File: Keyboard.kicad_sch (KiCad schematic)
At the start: 16 parts, among them J1 USB_mini_micro_B, SW1 SW_PUSH, U1 ATMEGA32U4, X1 XTAL_GND

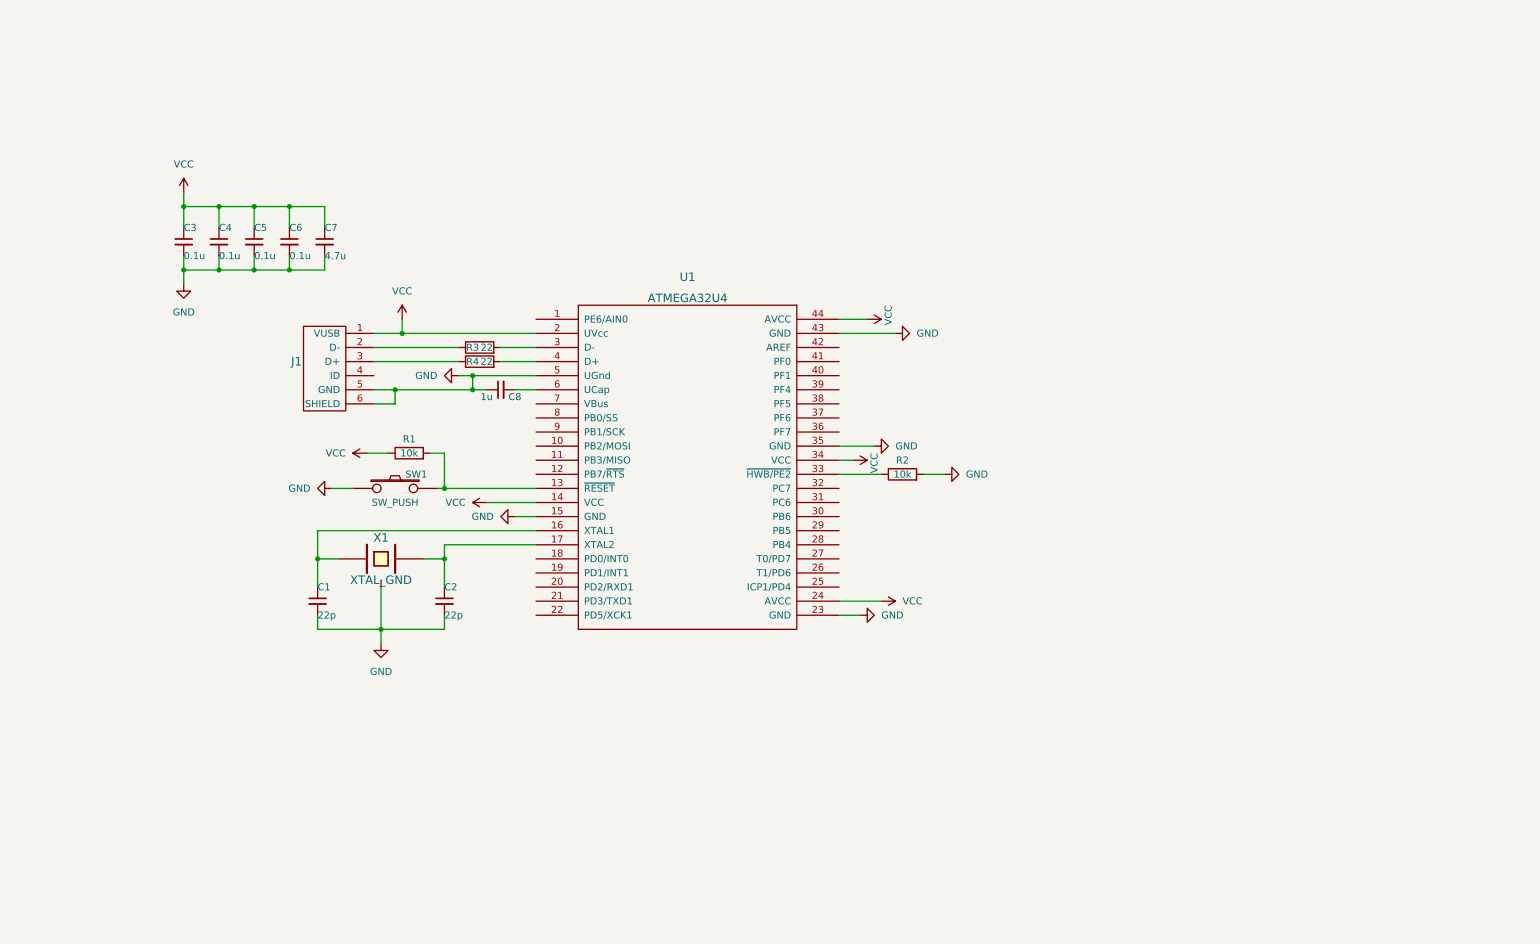
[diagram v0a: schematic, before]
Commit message: Added a TQFP pakcage version
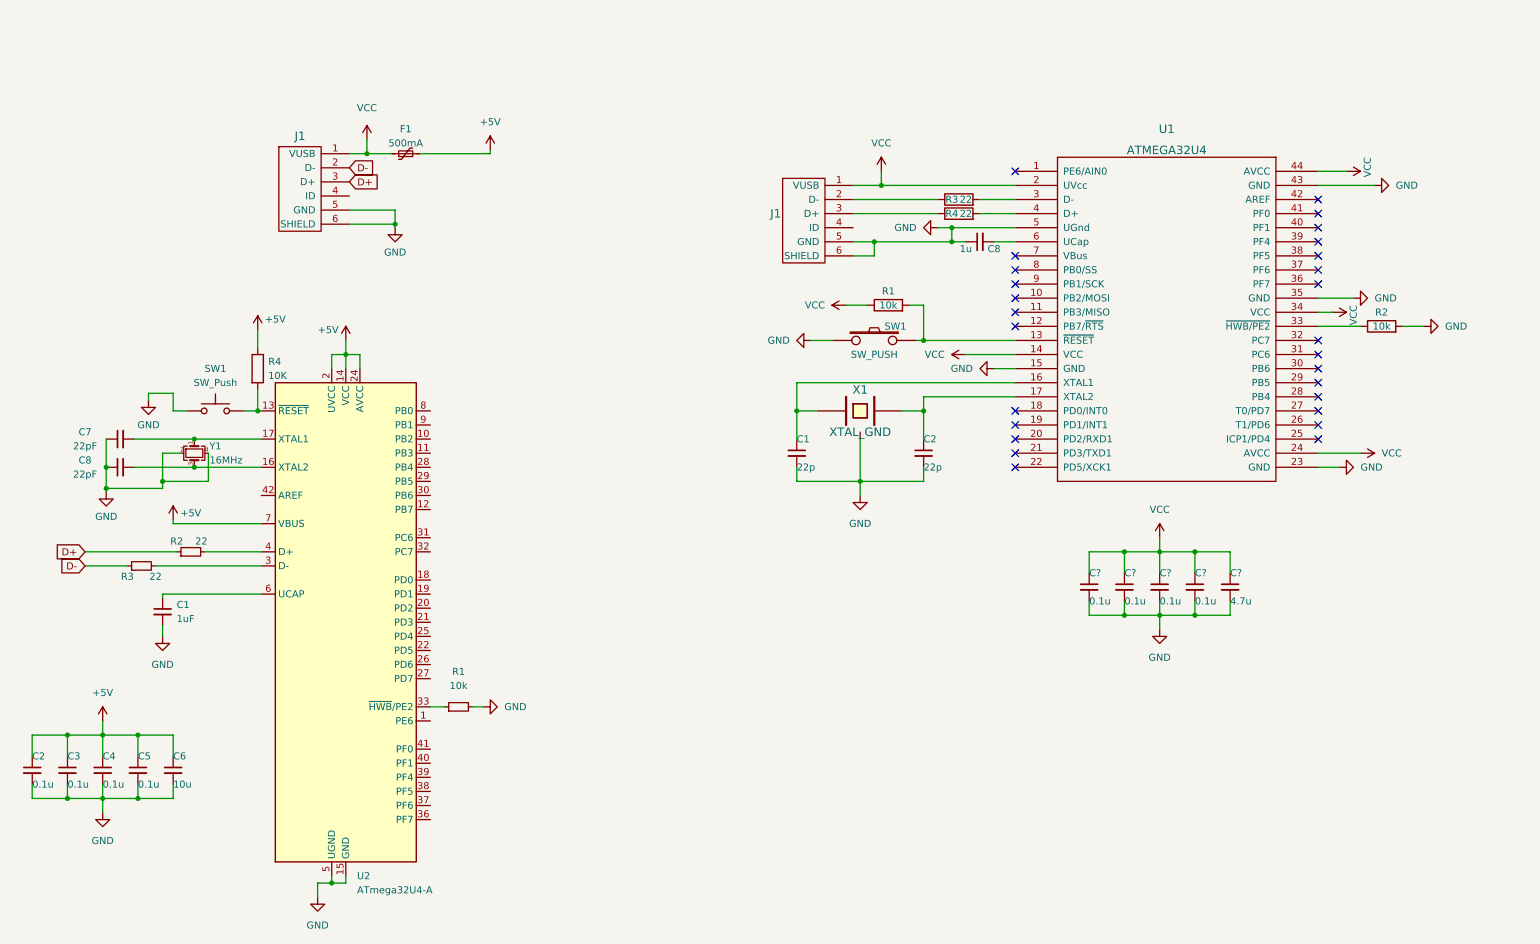
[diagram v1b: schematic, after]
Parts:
- added C1: 1uF, symbol Device:C_Small
- added C7, C8: 22pF, symbol Device:C_Small
- added C? (x4): 0.1u, symbol Device:C_Small
- added C?: 4.7u, symbol Device:C_Small
- added F1: 500mA, symbol Device:Polyfuse_Small
- added J1: USB_mini_micro_B, symbol keyboard_parts:USB_mini_micro_B
- added R1: 10k, symbol Device:R_Small
- added R2, R3: 22, symbol Device:R_Small
- added R4: 10K, symbol Device:R
- added SW1: SW_Push, symbol Switch:SW_Push
- added U2: ATmega32U4-A, Package_QFP:TQFP-44_10x10mm_P0.8mm, symbol MCU_Microchip_ATmega:ATmega32U4-A
- added Y1: 16MHz, symbol Device:Crystal_GND24_Small
- C6: renamed from C7; value 4.7u -> 10u
- renumbered C3 to C2, C4 to C3, C5 to C4, C6 to C5
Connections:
- net GND: now also C1.2, C7.1, C8.1, C?.2, C?.2, C?.2, C?.2, C?.2, J1.5 (GND), J1.6 (SHIELD), R1.2, SW1.1, U2.15 (GND), U2.23 (GND), U2.35 (GND), U2.43 (GND), U2.5 (UGND), Y1.2, Y1.4
- net VCC: now also C?.1, C?.1, C?.1, C?.1, C?.1, F1.1, J1.1 (VUSB); no longer C2.1, C3.1, C4.1, C5.1, C6.1
- new net: C7.2, U2.17 (XTAL1), Y1.1
- new net: R1.1, U2.33 (~{HWB}/PE2)
- new net: C8.2, U2.16 (XTAL2), Y1.3
- new net: R3.2, U2.3 (D-)
- new net: R2.2, U2.4 (D+)
- new net: R4.2, SW1.2, U2.13 (~{RESET})
- new net: C1.1, U2.6 (UCAP)
- new net +5V: C2.1, C3.1, C4.1, C5.1, C6.1, F1.2, R4.1, U2.14 (VCC), U2.2 (UVCC), U2.24 (AVCC), U2.34 (VCC), U2.44 (AVCC), U2.7 (VBUS)
- new net D+: J1.3 (D+), R2.1
- new net D-: J1.2 (D-), R3.1
- no-connect marks 0 -> 27
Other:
- moved on the sheet: C1, C2, C3, C4, C5, C6, C8, J1, R1, R2, R3, R4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

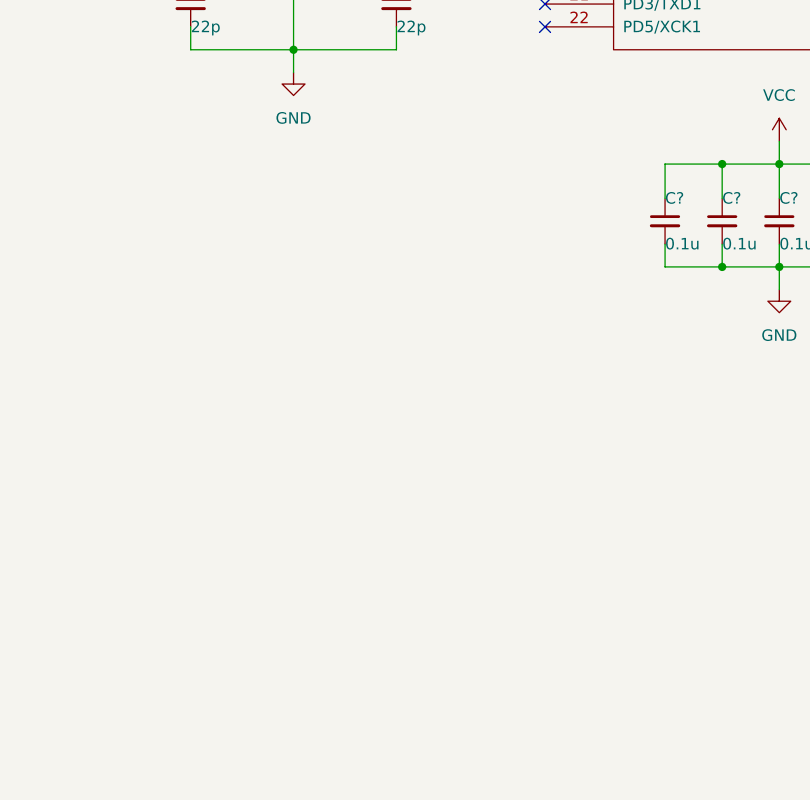
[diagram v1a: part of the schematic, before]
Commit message: Created Matrix file and added row and column wires
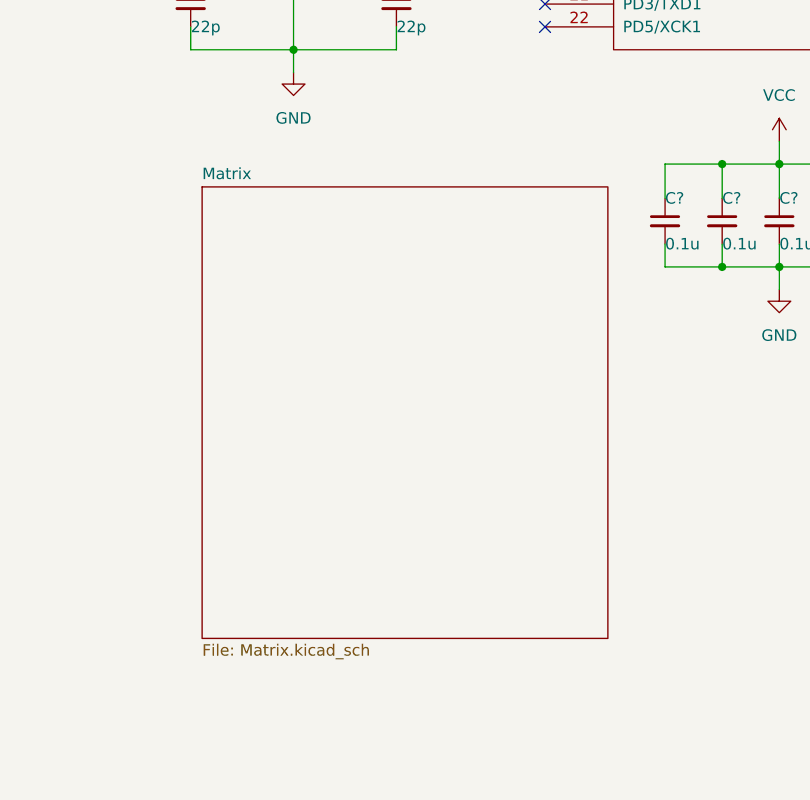
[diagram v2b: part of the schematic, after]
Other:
- added sheet Matrix (Matrix.kicad_sch)
- title: (none) -> main
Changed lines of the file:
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@@
 (kicad_sch (version 20211123) (generator eeschema)
   (paper "A4")
+  (title_block
+    (title "main")
+    (date "2022-08-09")
+    (rev "0")
+  )
   (junction (at 184.15 55.88) (diameter 0) (color 0 0 0 0)
   )
@@
     (pin "1")
   )
+  (sheet (at 157.48 114.3) (size 45.085 50.165) (fields_autoplaced)
+    (stroke (width 0.1524) (type solid) (color 0 0 0 0))
+    (fill (color 0 0 0 0.0000))
+    (property "Sheet name" "Matrix" (id 0) (at 157.48 113.5884 0)
+      (effects (font (size 1.27 1.27)) (justify left bottom))
+    )
+    (property "Sheet file" "Matrix.kicad_sch" (id 1) (at 157.48 165.0496 0)
+      (effects (font (size 1.27 1.27)) (justify left top))
+    )
+  )
   (sheet_instances
     (path "/" (page "1"))
+    (path "/c5d81d57-8916-4e7f-9cc3-b319fec74392" (page "2"))
   )
   (symbol_instances
@@
       (reference "C?") (unit 1) (value "0.1u") (footprint "")
     )
+    (path "/c5d81d57-8916-4e7f-9cc3-b319fec74392/6d39889c-9e2f-442a-a8e6-b65863b08f69"
+      (reference "D01") (unit 1) (value "1N4148") (footprint "")
+    )
     (path "/8545084e-b220-45d1-80e6-3744a0b67635"
       (reference "F1") (unit 1) (value "500mA") (footprint "")
@@
       (reference "R4") (unit 1) (value "10K") (footprint "")
     )
+    (path "/c5d81d57-8916-4e7f-9cc3-b319fec74392/0bbc6e45-febf-45ff-a858-5bf31f0a0486"
+      (reference "S01") (unit 1) (value "MX1A") (footprint "")
+    )
     (path "/6a7d6a80-4460-4050-abc5-328a82645129"

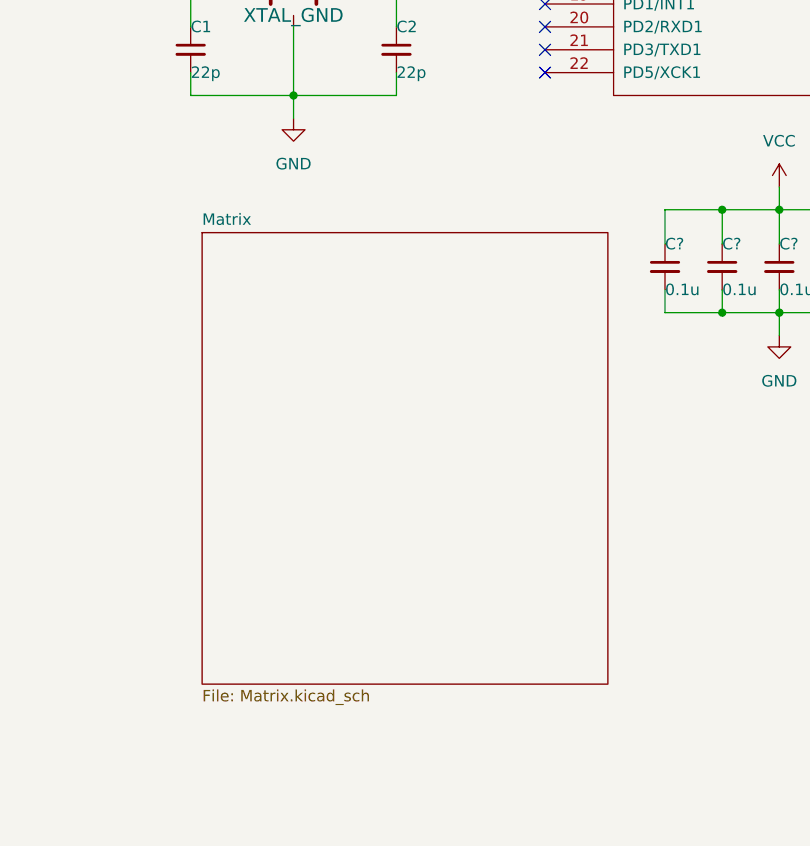
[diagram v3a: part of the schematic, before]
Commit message: Added key labels signifiying where each key will go to the matrix
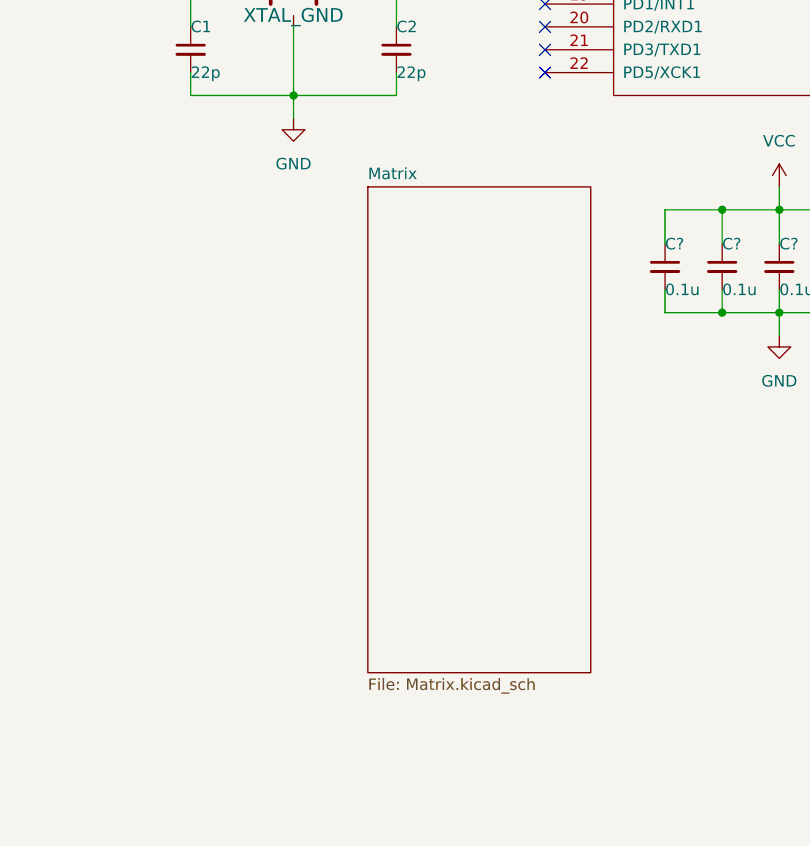
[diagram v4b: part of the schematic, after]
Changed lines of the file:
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@@
     (pin "1")
   )
-  (sheet (at 157.48 114.3) (size 45.085 50.165) (fields_autoplaced)
+  (sheet (at 175.895 109.22) (size 24.765 53.975) (fields_autoplaced)
     (stroke (width 0.1524) (type solid) (color 0 0 0 0))
     (fill (color 0 0 0 0.0000))
-    (property "Sheet name" "Matrix" (id 0) (at 157.48 113.5884 0)
+    (property "Sheet name" "Matrix" (id 0) (at 175.895 108.5084 0)
       (effects (font (size 1.27 1.27)) (justify left bottom))
     )
-    (property "Sheet file" "Matrix.kicad_sch" (id 1) (at 157.48 165.0496 0)
+    (property "Sheet file" "Matrix.kicad_sch" (id 1) (at 175.895 163.7796 0)
       (effects (font (size 1.27 1.27)) (justify left top))
     )
@@
       (reference "C?") (unit 1) (value "0.1u") (footprint "")
     )
-    (path "/c5d81d57-8916-4e7f-9cc3-b319fec74392/1946d543-a1f8-41d3-bbd2-336b3f685350"
+    (path "/c5d81d57-8916-4e7f-9cc3-b319fec74392/20346a50-9215-4897-b6eb-f263c4036474"
+      (reference "D?") (unit 1) (value "1N4148") (footprint "")
+    )
+    (path "/c5d81d57-8916-4e7f-9cc3-b319fec74392/3ea05721-74f1-4d12-82c8-1cd8c80d11c6"
+      (reference "D?") (unit 1) (value "1N4148") (footprint "")
+    )
+    (path "/c5d81d57-8916-4e7f-9cc3-b319fec74392/460164bc-dbe2-4808-92b2-d63df38aa859"
+      (reference "D?") (unit 1) (value "1N4148") (footprint "")
+    )
+    (path "/c5d81d57-8916-4e7f-9cc3-b319fec74392/5f0e13e3-ce63-4a14-bb2c-6230f1f0e675"
+      (reference "D?") (unit 1) (value "1N4148") (footprint "")
+    )
+    (path "/c5d81d57-8916-4e7f-9cc3-b319fec74392/64639e6f-1af0-4ecf-99cc-49756f014cd3"
       (reference "D?") (unit 1) (value "1N4148") (footprint "")
     )
     (path "/c5d81d57-8916-4e7f-9cc3-b319fec74392/6d39889c-9e2f-442a-a8e6-b65863b08f69"
+      (reference "D?") (unit 1) (value "1N4148") (footprint "")
+    )
+    (path "/c5d81d57-8916-4e7f-9cc3-b319fec74392/71ad471c-557d-4931-a34c-00f69c0e76c8"
+      (reference "D?") (unit 1) (value "1N4148") (footprint "")
+    )
+    (path "/c5d81d57-8916-4e7f-9cc3-b319fec74392/7cb3ba0e-a591-47ad-ad81-647171ed30ba"
+      (reference "D?") (unit 1) (value "1N4148") (footprint "")
+    )
+    (path "/c5d81d57-8916-4e7f-9cc3-b319fec74392/82db9459-1175-4e6f-b826-c4c06df8bdc3"
+      (reference "D?") (unit 1) (value "1N4148") (footprint "")
+    )
+    (path "/c5d81d57-8916-4e7f-9cc3-b319fec74392/82fb40b5-47df-44c8-9af3-070181c6e3ec"
+      (reference "D?") (unit 1) (value "1N4148") (footprint "")
+    )
+    (path "/c5d81d57-8916-4e7f-9cc3-b319fec74392/961983b1-18fc-4373-88cc-0d3c8ad0557a"
+      (reference "D?") (unit 1) (value "1N4148") (footprint "")
+    )
+    (path "/c5d81d57-8916-4e7f-9cc3-b319fec74392/a11210ef-eb5b-4940-a712-0ab57a862618"
+      (reference "D?") (unit 1) (value "1N4148") (footprint "")
+    )
+    (path "/c5d81d57-8916-4e7f-9cc3-b319fec74392/a63df499-4b65-4e7c-8764-35088ce4a7ac"
+      (reference "D?") (unit 1) (value "1N4148") (footprint "")
+    )
+    (path "/c5d81d57-8916-4e7f-9cc3-b319fec74392/ce009a1d-f86f-4f7f-855a-96a617e5ade2"
       (reference "D?") (unit 1) (value "1N4148") (footprint "")
     )
@@
       (reference "S?") (unit 1) (value "MX1A") (footprint "")
     )
-    (path "/c5d81d57-8916-4e7f-9cc3-b319fec74392/92d9c1c8-de76-4d24-99cb-0a6c6ce99dd9"
-      (reference "S?") (unit 1) (value "MX1A") (footprint "")
-    )
+    (path "/c5d81d57-8916-4e7f-9cc3-b319fec74392/13627275-fb64-40dd-8ef4-10f879245384"
+      (reference "S?") (unit 1) (value "MX1A") (footprint "")
+    )
+    (path "/c5d81d57-8916-4e7f-9cc3-b319fec74392/14cf79fe-cacc-4a2f-b420-ab59d3526c6a"
+      (reference "S?") (unit 1) (value "MX1A") (footprint "")
+    )
+    (path "/c5d81d57-8916-4e7f-9cc3-b319fec74392/298cf9e3-5a03-413a-88a3-5e8e299c879f"
+      (reference "S?") (unit 1) (value "MX1A") (footprint "")
+    )
+    (path "/c5d81d57-8916-4e7f-9cc3-b319fec74392/361aa8b5-d6ec-481f-9644-111eb0fe31fa"
+      (reference "S?") (unit 1) (value "MX1A") (footprint "")
+    )
+    (path "/c5d81d57-8916-4e7f-9cc3-b319fec74392/5ec519c2-c7eb-42eb-a270-cccb7f70ef3e"
+      (reference "S?") (unit 1) (value "MX1A") (footprint "")
+    )
+    (path "/c5d81d57-8916-4e7f-9cc3-b319fec74392/772dbc6e-66ae-4648-a967-d678917a153c"
+      (reference "S?") (unit 1) (value "MX1A") (footprint "")
+    )
+    (path "/c5d81d57-8916-4e7f-9cc3-b319fec74392/784a4307-1bc2-40bf-831d-d0fa00e25954"
+      (reference "S?") (unit 1) (value "MX1A") (footprint "")
+    )
+    (path "/c5d81d57-8916-4e7f-9cc3-b319fec74392/80edb857-6e0d-45e9-aeff-e6dc163b2a6c"
+      (reference "S?") (unit 1) (value "MX1A") (footprint "")
+    )
+    (path "/c5d81d57-8916-4e7f-9cc3-b319fec74392/b52e57f1-d814-459a-b0c6-7e57b07bf92a"
+      (reference "S?") (unit 1) (value "MX1A") (footprint "")
+    )
+    (path "/c5d81d57-8916-4e7f-9cc3-b319fec74392/db34a3e2-518e-4263-9b7d-5fae152e65d9"
+      (reference "S?") (unit 1) (value "MX1A") (footprint "")
+    )
+    (path "/c5d81d57-8916-4e7f-9cc3-b319fec74392/f01e4114-0f51-4334-906b-a36272d3aef3"
+      (reference "S?") (unit 1) (value "MX1A") (footprint "")
+    )
+    (path "/c5d81d57-8916-4e7f-9cc3-b319fec74392/f3b946d3-65b2-4d7e-97c4-21b8a257f460"
+      (reference "S?") (unit 1) (value "MX1A") (footprint "")
+    )
+    (path "/c5d81d57-8916-4e7f-9cc3-b319fec74392/fcd1ee04-863c-4d34-a243-22dd5e59993b"
+      (reference "S?") (unit 1) (value "MX1A") (footprint "")
+    )
